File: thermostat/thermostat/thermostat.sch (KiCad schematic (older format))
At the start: 30 parts, among them SW1 SW_Push, SW2 SW_Push, SW3 SW_Push, SW4 SW_Push, SW5 SW_Push, SW6 SW_Push, SW7 SW_Push, SW8 SW_Push, U1 UG-2864HSWEG01, U2 WeMos_mini, U3 MCP23017

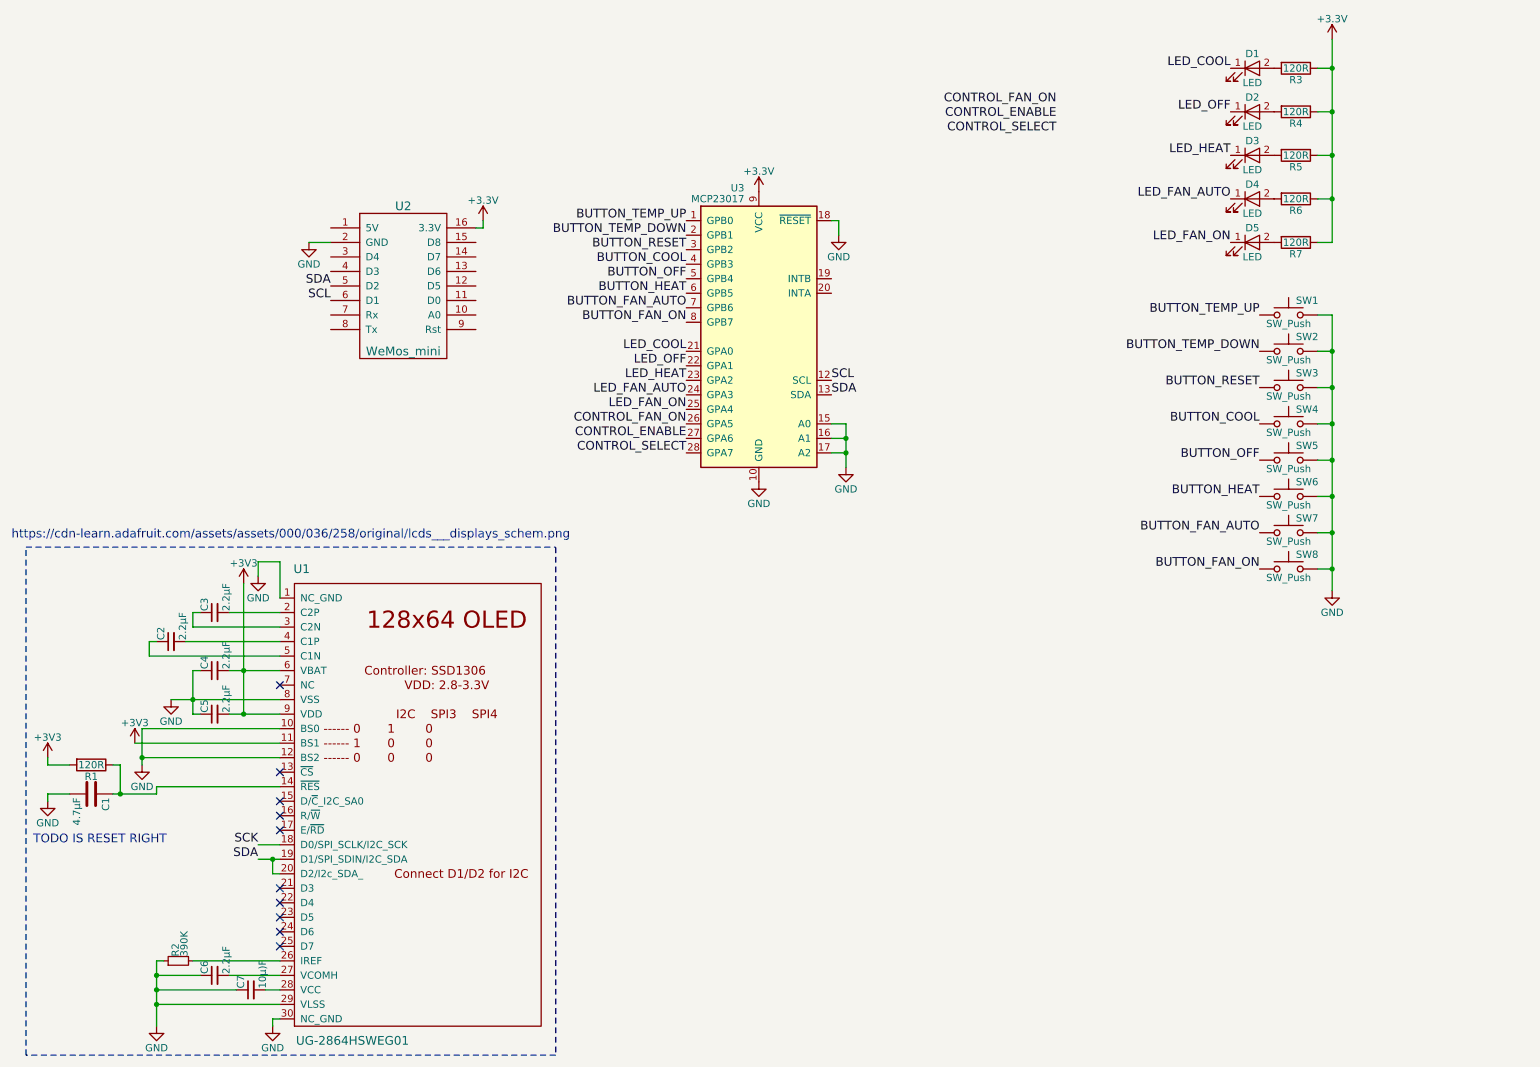
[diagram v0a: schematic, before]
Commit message: Thermostat V2 board/code; atmosphere sensor board/code; kicad libs
thermostat uses mcp23017, also fixed cooling logic?

Commit d1_mini_kicad library sumodule as files instead of sumodule

git@github.com:jerome-labidurie/d1_mini_kicad.git

update thermostat kicad stuff for new libs

thermostat: finish schematic and start layout

Layout progress

Thermostat sent to board house

Thermostat v1.1 + code to match v1/v1.1

Thermostat code needed updating to match board

thermostat comments

thermostat display NC for no temp sensor

small changes to next version thermostat board

fix themostat board maybe

Test board with breadboard; fix board and logic

Thermostat v2 routing first pass

Thermostat pcb now has the cuttable debug traces for 74xx logic

Thermostat cleanup for board production

Thermostat mounting holes

kicad libs to common dir; create atmosphere sensor board

atmosphere board move bme280

atmosphere sensor board something hcanged

fix logo on thermostat, boards ordered

Atmosphere sensor code only uses BME280; has error for disconnected

Thermostat fix bme280 error message topic

force fan on for cool; logo

Debug print fixes

Thermostat print cleanup; connected logo

force fan on for heat

Add HEAT_ONLY flag; mqtt stat reporting

handle no bme280 by assuming 10, display that
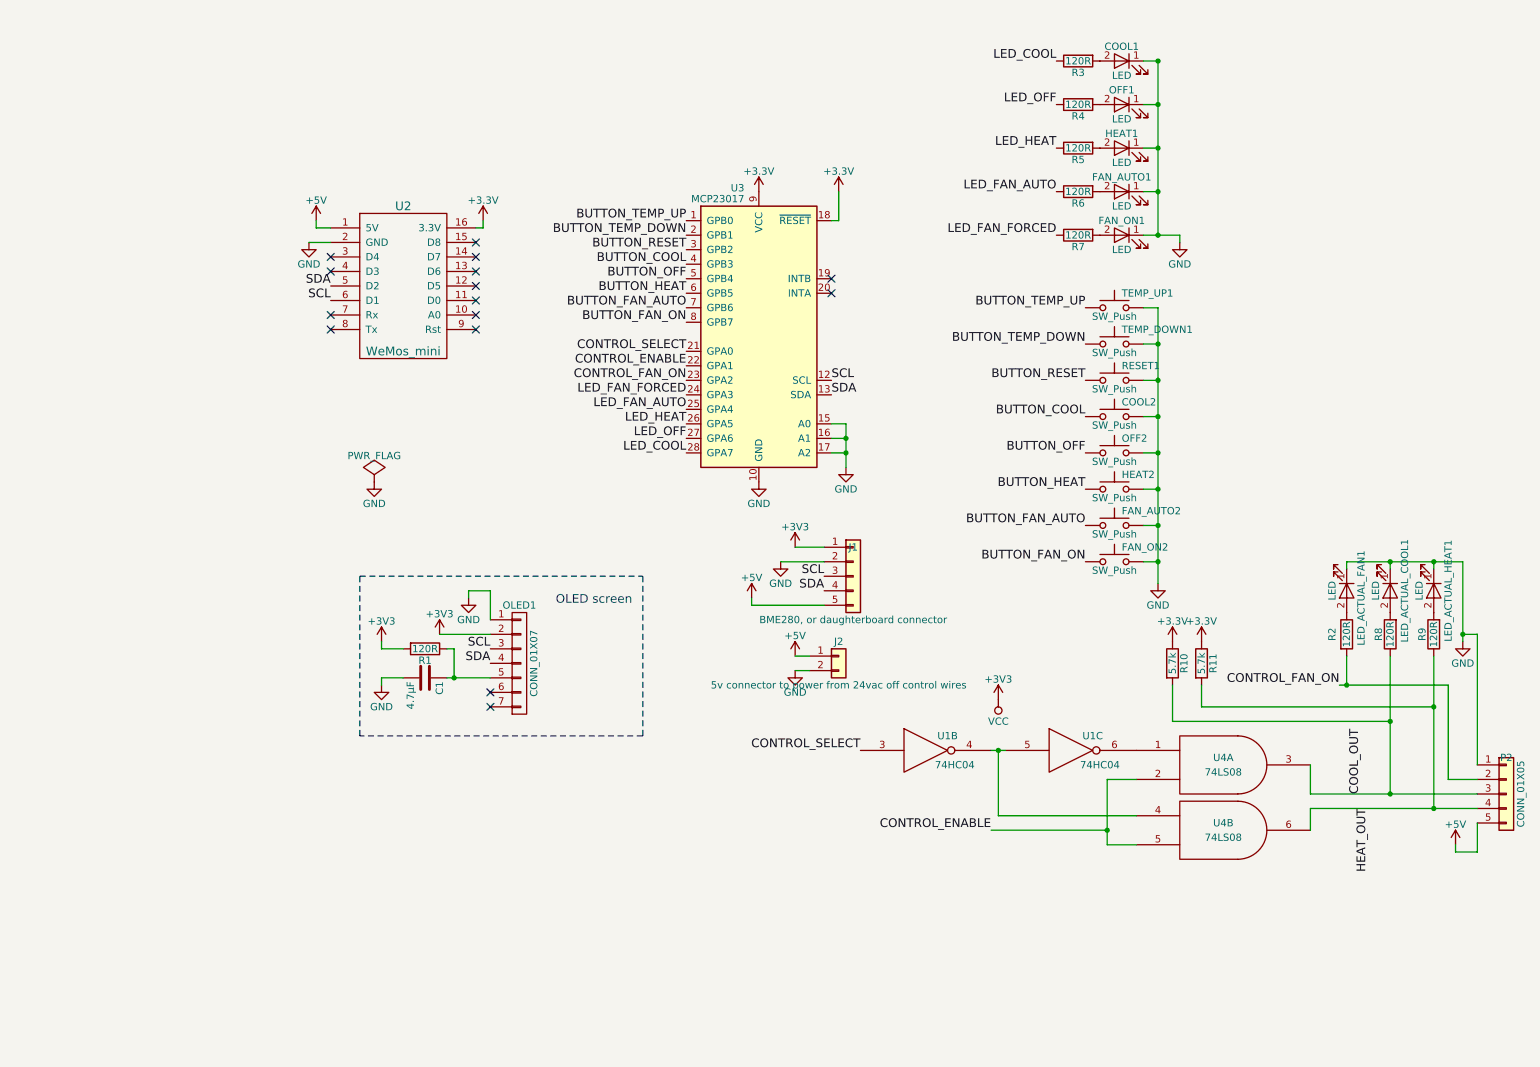
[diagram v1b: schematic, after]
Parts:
- removed C2, C3, C4, C5, C6: 2.2µF, Capacitors_THT:C_Disc_D3.8mm_W2.6mm_P2.50mm, symbol C_Small
- removed C7: 10µ)F, Capacitors_THT:C_Disc_D3.8mm_W2.6mm_P2.50mm, symbol C_Small
- removed R2: 390K, Resistors_THT:R_Axial_DIN0204_L3.6mm_D1.6mm_P2.54mm_Vertical, symbol R_Small
- removed U1: UG-2864HSWEG01, mine:UG-2864HSWEG01, symbol UG-2864HSWEG01
- added J1: BME280, or daughterboard connector, Pin_Headers:Pin_Header_Straight_1x05, symbol Conn_01x05
- added J2: 5v connector to power from 24vac off control wires, Pin_Headers:Pin_Header_Straight_1x02, symbol Conn_01x02
- added LED_ACTUAL_COOL1, LED_ACTUAL_FAN1, LED_ACTUAL_HEAT1: LED, LEDs:LED_D3.0mm, symbol LED
- added OLED1: CONN_01X07, mine:OLED_I2C_SPI, symbol CONN_01X07
- added P2: CONN_01X05, Pin_Headers:Pin_Header_Straight_1x05, symbol Conn_01x05
- added R10, R11: 5.7k, Resistors_SMD:R_0603_HandSoldering, symbol R
- added R2, R8, R9: 120R, Resistors_SMD:R_0603_HandSoldering, symbol R
- added U1: 74HC04, Housings_DIP:DIP-14_W7.62mm, symbol 74HC04
- added U4: 74LS08, mine:DIP-14_W7.62mm_cuttable-trace, symbol 74LS08
- C1: footprint Capacitors_THT:C_Disc_D3.8mm_W2.6mm_P2.50mm -> Capacitors_SMD:C_0603_HandSoldering
- COOL2: renamed from SW4; footprint (none) -> Buttons_Switches_ThroughHole:SW_Tactile_SPST_Angled
- FAN_AUTO2: renamed from SW7; footprint (none) -> Buttons_Switches_THT:SW_PUSH_6mm
- FAN_ON2: renamed from SW8; footprint (none) -> Buttons_Switches_THT:SW_PUSH_6mm
- HEAT2: renamed from SW6; footprint (none) -> Buttons_Switches_ThroughHole:SW_Tactile_SPST_Angled
- OFF2: renamed from SW5; footprint (none) -> Buttons_Switches_ThroughHole:SW_Tactile_SPST_Angled
- R1, R3, R4, R5, R6, R7: footprint Resistors_THT:R_Axial_DIN0204_L3.6mm_D1.6mm_P2.54mm_Vertical -> Resistors_SMD:R_0603_HandSoldering
- RESET1: renamed from SW3; footprint (none) -> Buttons_Switches_THT:SW_PUSH_6mm
- TEMP_DOWN1: renamed from SW2; footprint (none) -> Buttons_Switches_THT:SW_PUSH_6mm
- TEMP_UP1: renamed from SW1; footprint (none) -> Buttons_Switches_THT:SW_PUSH_6mm
- renumbered D1 to COOL1, D4 to FAN_AUTO1, D5 to FAN_ON1, D3 to HEAT1, D2 to OFF1
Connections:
- net +3V3: now also U3.18 (~RESET), J1.1 (Pin_1), OLED1.2 (P2), R10.1, R11.1, U1.14 (VCC), U1.14 (VCC), U4.14 (VCC), U4.14 (VCC); no longer R3.1, R4.1, R5.1, R6.1, R7.1
- net CONTROL_ENABLE: now also U3.22 (GPA1), U4.2, U4.5; no longer U3.27 (GPA6)
- net CONTROL_FAN_ON: now also U3.23 (GPA2), P2.2 (Pin_2), R2.2; no longer U3.26 (GPA5)
- net CONTROL_SELECT: now also U3.21 (GPA0), U1.3; no longer U3.28 (GPA7)
- net GND: now also COOL1.1 (K), FAN_AUTO1.1 (K), FAN_ON1.1 (K), HEAT1.1 (K), OFF1.1 (K), J1.2 (Pin_2), J2.2 (Pin_2), LED_ACTUAL_COOL1.1 (K), LED_ACTUAL_FAN1.1 (K), LED_ACTUAL_HEAT1.1 (K), OLED1.1 (P1), P2.1 (Pin_1), U1.7 (GND), U1.7 (GND), U4.7 (GND), U4.7 (GND); no longer U3.18 (~RESET)
- net LED_COOL: now also R3.1, U3.28 (GPA7); no longer COOL1.1 (K), U3.21 (GPA0)
- net LED_FAN_AUTO: now also R6.1, U3.25 (GPA4); no longer FAN_AUTO1.1 (K), U3.24 (GPA3)
- net LED_HEAT: now also R5.1, U3.26 (GPA5); no longer HEAT1.1 (K), U3.23 (GPA2)
- net LED_OFF: now also R4.1, U3.27 (GPA6); no longer OFF1.1 (K), U3.22 (GPA1)
- net SCL: now also J1.3 (Pin_3), OLED1.3 (P3)
- net SDA: now also J1.4 (Pin_4), OLED1.4 (P4)
- net +5V: now reaches U2.1 (5V)
- net +5V: now also J1.5 (Pin_5), J2.1 (Pin_1), P2.5 (Pin_5)
- net at C1.1, R1.1: now also OLED1.5 (P5)
- removed net LED_FAN_ON: FAN_ON1.1 (K), U3.25 (GPA4)
- new net: U1.4, U1.5, U4.4
- new net: U1.6, U4.1
- new net: LED_ACTUAL_FAN1.2 (A), R2.1
- new net: LED_ACTUAL_COOL1.2 (A), R8.2
- new net: LED_ACTUAL_HEAT1.2 (A), R9.2
- new net COOL_OUT: P2.3 (Pin_3), R10.2, R8.1, U4.3
- new net HEAT_OUT: P2.4 (Pin_4), R11.2, R9.1, U4.6
- new net LED_FAN_FORCED: R7.1, U3.24 (GPA3)
- no-connect marks 10 -> 15
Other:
- note added: "OLED screen"
- note removed: "TODO IS RESET RIGHT\n"
- note removed: "https://cdn-learn.adafruit.com/assets/assets/000/036/258/original/lcds___displays_schem.png"
- moved on the sheet: C1, COOL1, COOL2, FAN_AUTO1, FAN_AUTO2, FAN_ON1, FAN_ON2, HEAT1, HEAT2, OFF1, OFF2, R1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
